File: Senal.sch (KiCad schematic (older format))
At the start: 0 parts

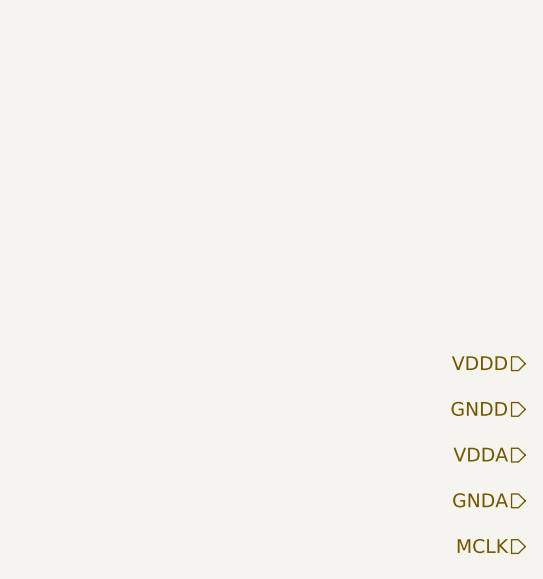
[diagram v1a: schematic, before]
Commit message: Se terminaron todos los simbolos necesarios. Se realizo el esquematico de la fuente y el reloj. Se inicio el esquematico de la parte de señal.
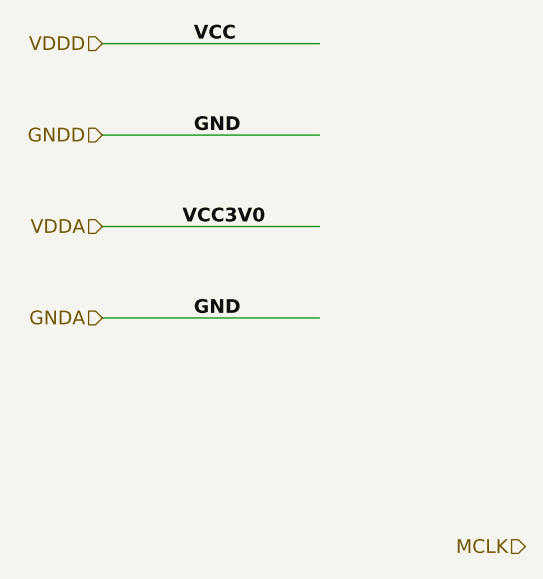
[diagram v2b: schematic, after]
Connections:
- net labels added: GND, VCC, VCC3V0
- wire segments 0 -> 4
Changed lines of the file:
@@
 LIBS:contrib
 LIBS:valves
+LIBS:PMOD_IA
 LIBS:proyectoDCI-cache
 EELAYER 25 0
@@
 $Descr A4 11693 8268
 encoding utf-8
-Sheet 3 4
+Sheet 2 4
 Title ""
 Date ""
@@
 Comment4 ""
 $EndDescr
-Text HLabel 3050 2300 0    60   Input ~ 0
+Text HLabel 1200 900  0    60   Input ~ 0
 VDDD
-Text HLabel 3050 2500 0    60   Input ~ 0
+Text HLabel 1200 1300 0    60   Input ~ 0
 GNDD
-Text HLabel 3050 2700 0    60   Input ~ 0
+Text HLabel 1200 1700 0    60   Input ~ 0
 VDDA
-Text HLabel 3050 2900 0    60   Input ~ 0
+Text HLabel 1200 2100 0    60   Input ~ 0
 GNDA
 Text HLabel 3050 3100 0    60   Input ~ 0
 MCLK
+Wire Wire Line
+	1200 900  2150 900
+Wire Wire Line
+	1200 1300 2150 1300
+Wire Wire Line
+	1200 1700 2150 1700
+Wire Wire Line
+	1200 2100 2150 2100
+Text Label 1600 900  0    60   ~ 12
+VCC
+Text Label 1600 1300 0    60   ~ 12
+GND
+Text Label 1550 1700 0    60   ~ 12
+VCC3V0
+Text Label 1600 2100 0    60   ~ 12
+GND
 $EndSCHEMATC

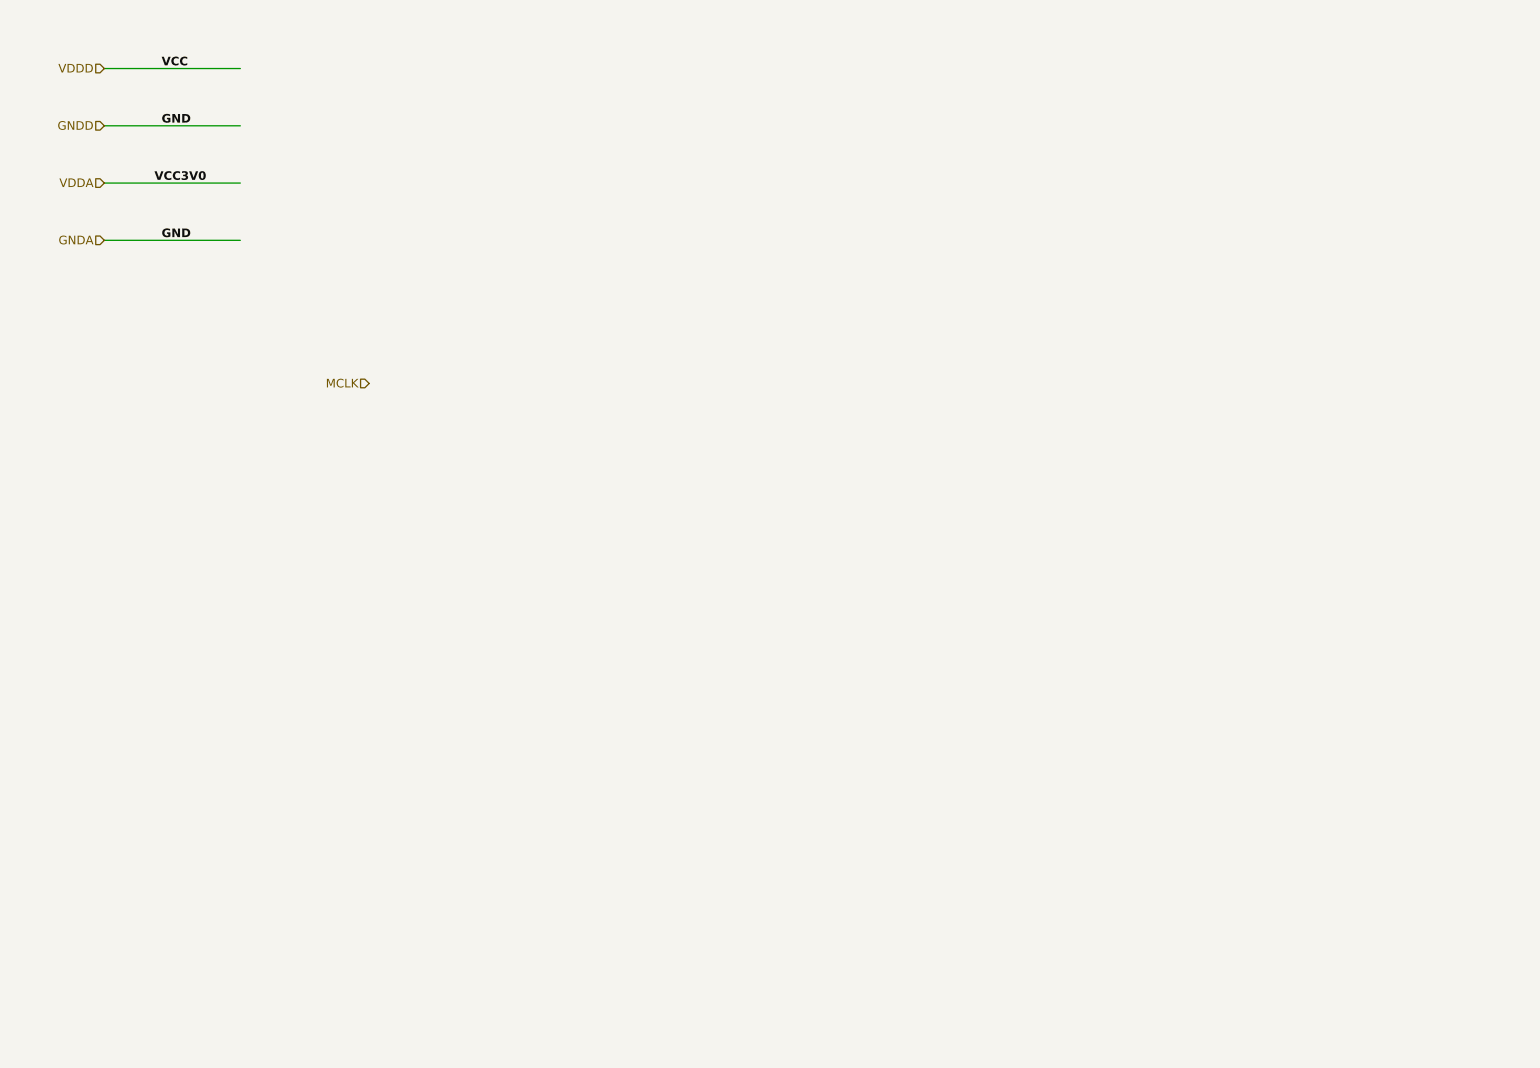
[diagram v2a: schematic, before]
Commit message: Se trabajo sobre la hoja de señal. Se terminó el esquemático, salvo que resta agregar los conectores.
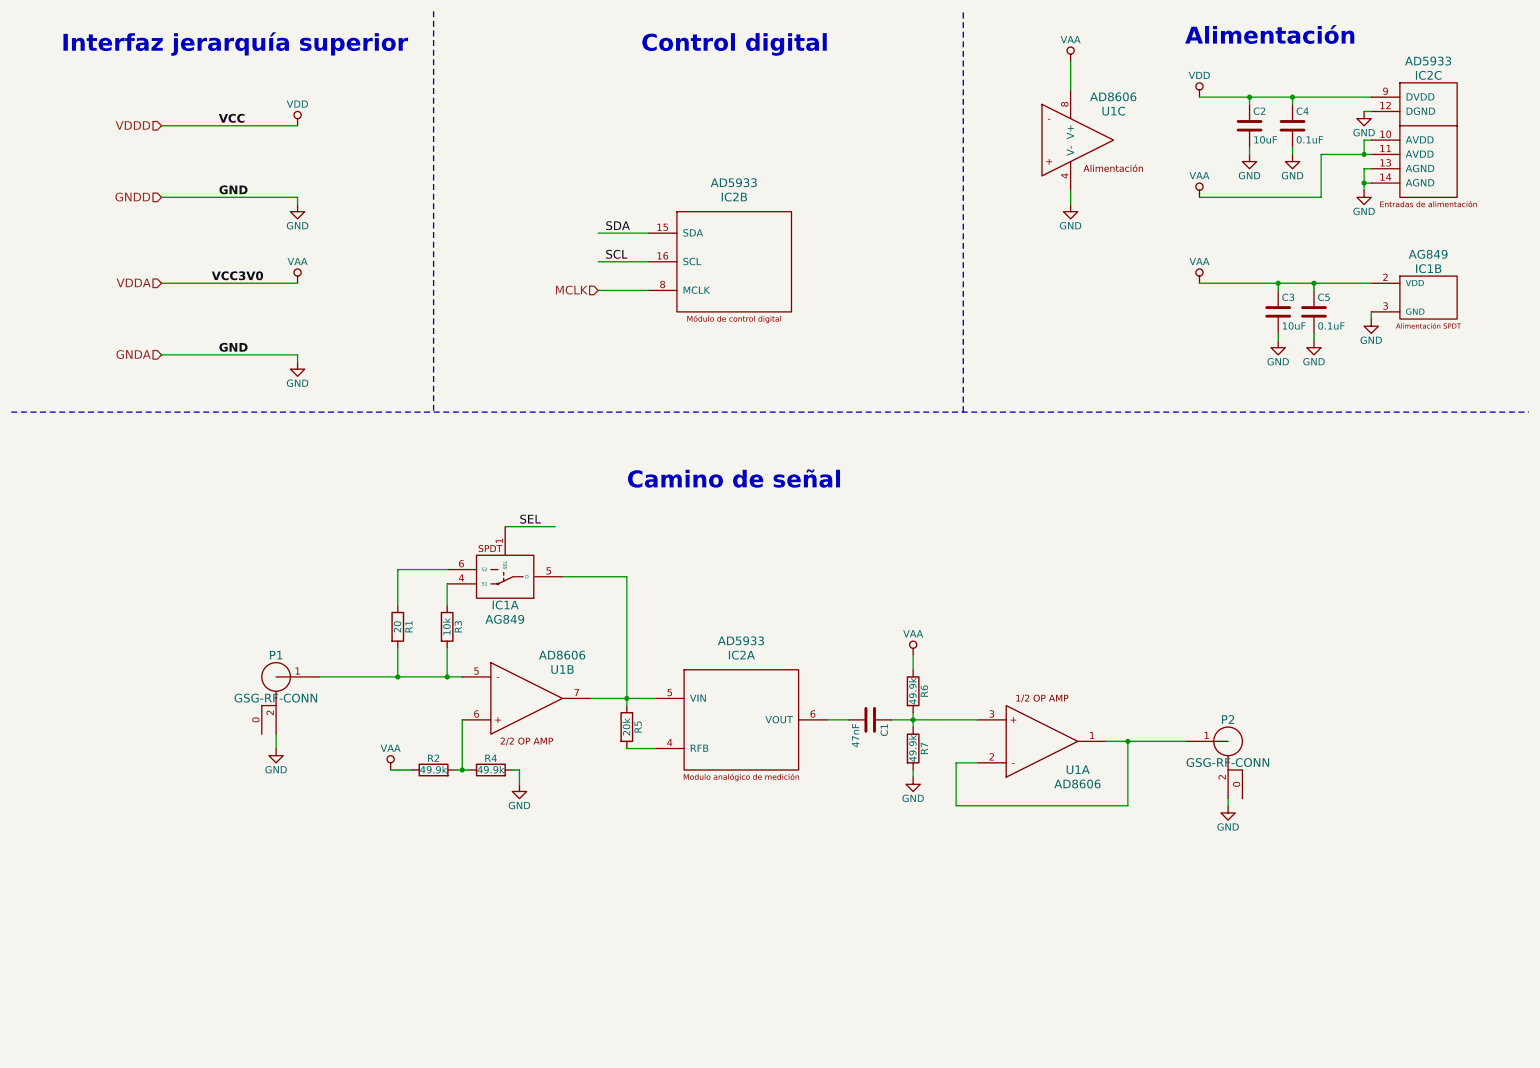
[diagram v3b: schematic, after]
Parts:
- added C1: 47nF, symbol C
- added C2, C3: 10uF, symbol C
- added C4, C5: 0.1uF, symbol C
- added IC1: AG849, symbol AG849
- added IC2: AD5933, symbol AD5933
- added P1, P2: GSG-RF-CONN, symbol GSG-RF-CONN
- added R1: 20, symbol R
- added R2, R4, R6, R7: 49.9k, symbol R
- added R3: 10k, symbol R
- added R5: 20k, symbol R
- added U1: AD8606, symbol AD8606
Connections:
- net labels added: SCL, SDA, SEL, VAA, VDD
- wire segments 4 -> 73
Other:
- note added: "Alimentación"
- note added: "Camino de señal"
- note added: "Control digital"
- note added: "Interfaz jerarquía superior"

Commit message: Agregados los conectores. Finalizado el esquemático
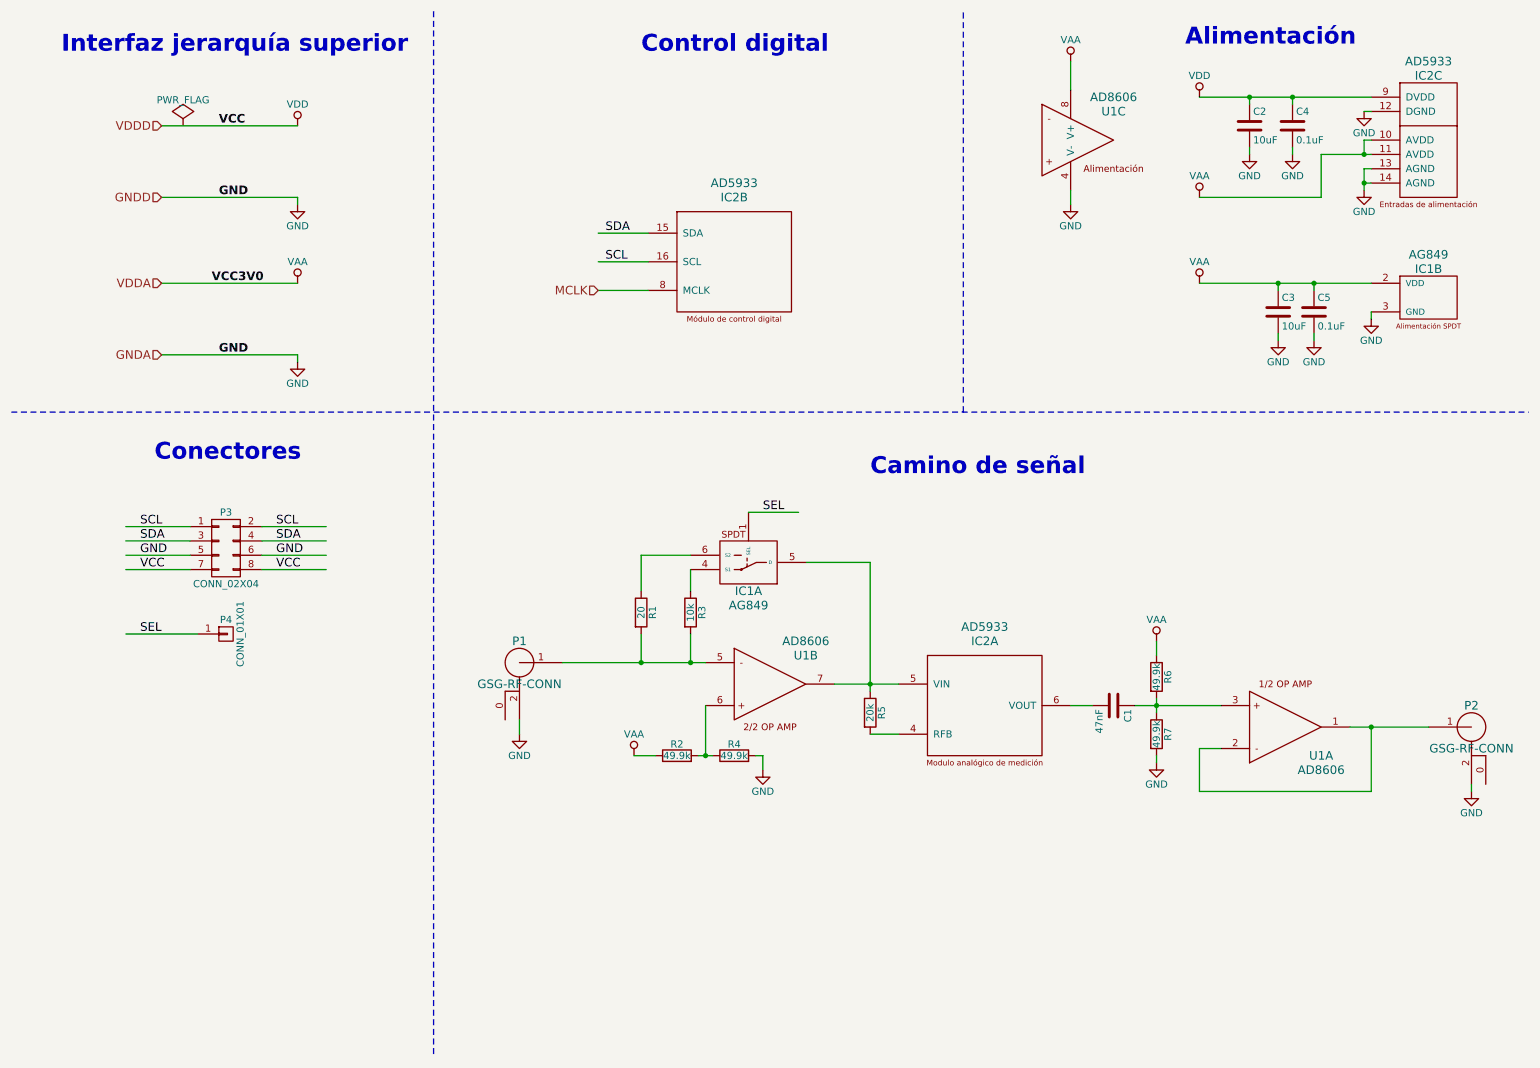
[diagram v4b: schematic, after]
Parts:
- added P3: CONN_02X04, symbol CONN_02X04
- added P4: CONN_01X01, symbol CONN_01X01
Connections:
- wire segments 73 -> 68
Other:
- note added: "Conectores"
- moved on the sheet: C1, IC1A, IC2A, P1, P2, R1, R2, R3, R4, R5, R6, R7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

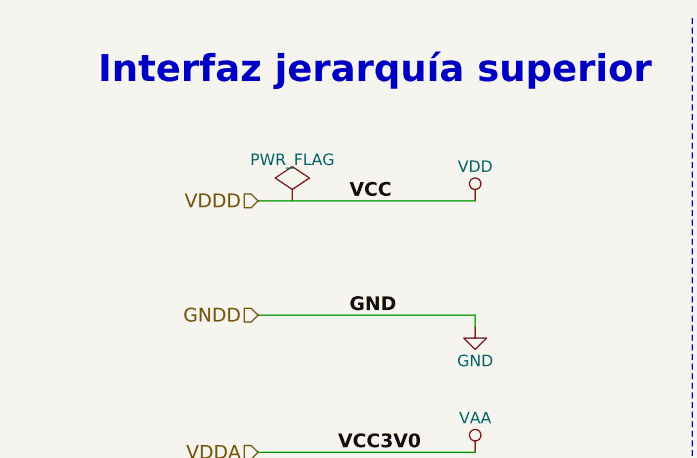
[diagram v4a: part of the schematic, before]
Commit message: Se enlazaron los simbolos con los footprint. Se agregó una librería con conectores SMA.
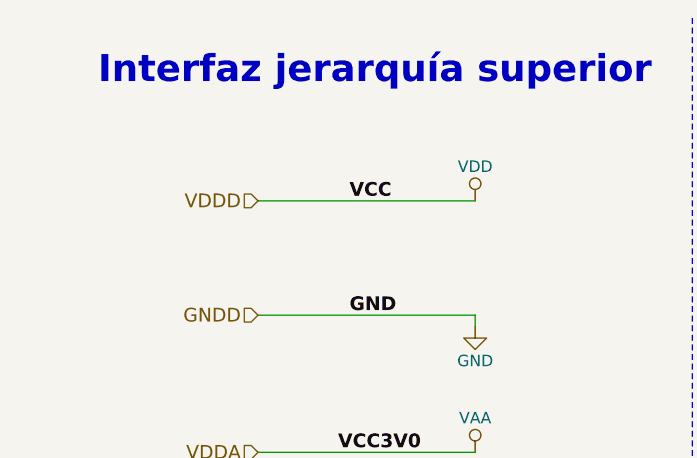
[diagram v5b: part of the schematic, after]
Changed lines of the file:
@@
 Text Notes 1550 3650 0    118  ~ 24
 Conectores
-$Comp
-L PWR_FLAG #FLG?
-U 1 1 58382427
-P 1750 1300
-F 0 "#FLG?" H 1750 1395 50  0001 C CNN
-F 1 "PWR_FLAG" H 1750 1480 50  0000 C CNN
-F 2 "" H 1750 1300 50  0000 C CNN
-F 3 "" H 1750 1300 50  0000 C CNN
-	1    1750 1300
-	1    0    0    -1
-$EndComp
 $EndSCHEMATC
